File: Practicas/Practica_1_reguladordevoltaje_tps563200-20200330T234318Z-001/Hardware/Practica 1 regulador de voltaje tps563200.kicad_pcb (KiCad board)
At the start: 2 copper layers, 50 x 20 mm, 12 parts, among them J1 Screw_Terminal_01x02, J2 Screw_Terminal_01x02, U1 TPS563200

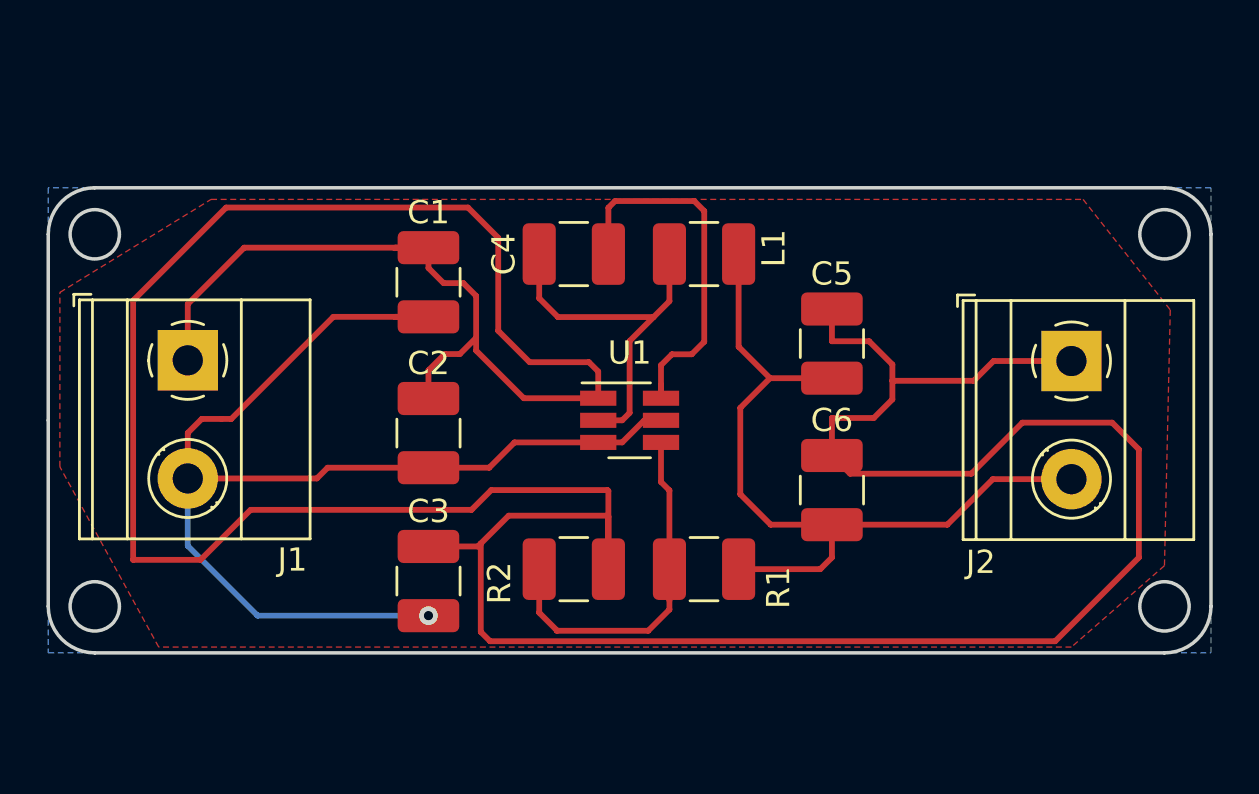
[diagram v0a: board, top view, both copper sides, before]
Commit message: P1 Version 2.0: se realizo el ruteado con el uso de los planos, escribir texto e insertar logos o simbologia en forma de huellas
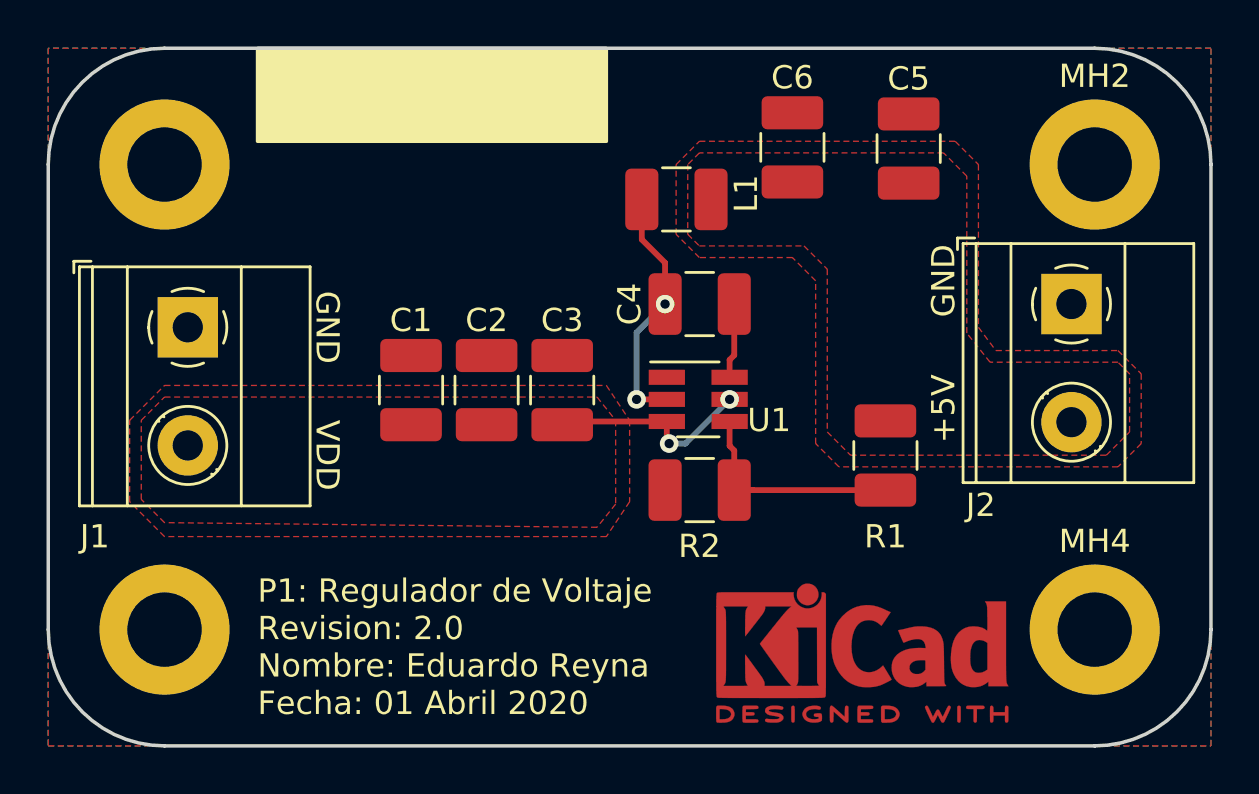
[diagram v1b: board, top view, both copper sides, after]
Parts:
- added MH1: MountingHole_Pad, MountingHole:MountingHole_3.2mm_M3_DIN965_Pad, F.Cu at (117.0, 81.0)
- added MH2: MountingHole_Pad, MountingHole:MountingHole_3.2mm_M3_DIN965_Pad, F.Cu at (157.0, 81.0)
- added MH3: MountingHole_Pad, MountingHole:MountingHole_3.2mm_M3_DIN965_Pad, F.Cu at (117.0, 101.0)
- added MH4: MountingHole_Pad, MountingHole:MountingHole_3.2mm_M3_DIN965_Pad, F.Cu at (157.0, 101.0)
- added REF**: KiCad-Logo2_5mm_Copper, Symbol:KiCad-Logo2_5mm_Copper, F.Cu at (147.0, 102.0)
- moved C6 14.8 mm to (144.0, 80.3)
- moved C3 10.0 mm to (134.1, 90.7)
- moved R1 9.20 mm to (148.0, 93.5), turned to 270 degrees
- moved C5 9.01 mm to (149.0, 80.3)
- moved R2 6.39 mm to (140.0, 95.0), turned to 180 degrees
- moved C4 5.82 mm to (140.0, 87.0)
- moved C1 4.70 mm to (127.6, 90.7)
- moved C2 3.11 mm to (130.8, 90.7)
- moved U1 3.08 mm to (139.9, 91.1)
- moved L1 2.63 mm to (139.0, 82.5)
- moved J2 2.45 mm to (156.0, 87.0)
- moved J1 1.42 mm to (118.0, 88.0)
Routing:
- net GND: track 177.6 -> 0.00 mm
- net VDD: track 51.9 -> 9.24 mm, vias 1 -> 2
- net +5V: track 35.3 -> 0.00 mm
- net Net-(C4-Pad2): track 16.3 -> 3.23 mm
- net Net-(R1-Pad2): track 16.9 -> 9.53 mm
- net Net-(C4-Pad1): track 16.2 -> 10.8 mm, vias 0 -> 2
- added copper zone on F.Cu, net +5V
- added copper zone on F.Cu, net VDD
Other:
- board size 50 x 20 mm -> 50 x 30 mm
- board text added: "+5V"
- board text added: "GND"
- board text added: "P1: Regulador de Voltaje Revision: 2.0 Nombre: Eduardo Reyna Fecha: 01 Abril 2020"
- board text added: "VDD"
